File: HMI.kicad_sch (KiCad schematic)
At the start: 180 parts, among them J702 1050171001 Micro Type B, J703 Conn_01x04_Pin, J704 Conn_01x04_Pin, J705 Conn_01x14_Pin, J706 Header, J707 HX JN1.27-2x5 WZ H4.9, J708 HX JN1.27-2x5 WZ H4.9, SW701 EncSw, SW702 EncSw, SW703 EncSw, U701 STM32G431K8Tx, Y701 20 MHz

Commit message: Refactoring sch
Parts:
- removed P707: ~, symbol personal:Cosmetic_PWR_SRC
- removed P708: ~, symbol personal:Cosmetic_OUT
- removed P709, P712, P713: ~, symbol personal:Cosmetic_IN
- removed P711: ~, symbol personal:Cosmetic_IO
- removed P717, P718: ~, symbol personal:Cosmetic_GND2
- added J701: ZHOURI DC3, Connector_IDC:IDC-Header_2x05_P2.54mm_Horizontal, symbol Connector_Generic:Conn_02x05_Odd_Even
- added JP701: 0R, Resistor_THT:R_Axial_DIN0204_L3.6mm_D1.6mm_P5.08mm_Horizontal, symbol Device:R
- added P1: ~, symbol personal:Cosmetic_PWR
- added P10, P11, P2, P9: ~, symbol personal:Cosmetic_GND2
- added P3: ~, symbol personal:Cosmetic_PWR_SRC
- added P4: ~, symbol personal:Cosmetic_OUT
- added P5, P7, P8: ~, symbol personal:Cosmetic_IN
- added P6: ~, symbol personal:Cosmetic_IO
- added R701: 10k, Resistor_SMD:R_0603_1608Metric_Pad0.98x0.95mm_HandSolder, symbol Device:R
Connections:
- net Earth: now also JP701.2
- net GND: now also J701.5 (Pin_5), P10.1, P11.1, P2.1, P9.1
- net LV_NRST: now also J701.9 (Pin_9), P8.1, R701.2
- net LV_RX: now also J701.1 (Pin_1), P4.1
- net LV_SWDCLK: now also J701.10 (Pin_10), P7.1
- net LV_SWDIO: now also J701.8 (Pin_8), P6.1
- net LV_TX: now also J701.3 (Pin_3), P5.1
- net SL3: now also J701.6 (Pin_6), P1.1, P3.1, R701.1
- new net: J701.2 (Pin_2), JP701.1
- no-connect marks 9 -> 11
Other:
- note added: "INTERFACE TO MAIN BOARD"
- note added: "SWD header - Main board"
- note removed: "BLOCK INTERFACE"
- note removed: "SWD header - Main"
- moved on the sheet: C701, C702, C703, C704, C705, C706, C707, C708, C709, C711, C712, J706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

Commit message: sch refactoring complete
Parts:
- removed P10, P11, P2, P710, P719, P720, P721, P722, P723, P724, P725, P726, P727, P735, P737, P738, P740, P741, P742, P743, P778, P779, P780, P783, P785, P787, P788, P795, P796, P797, P798, P806, P9: ~, symbol personal:Cosmetic_GND2
- added H701, H702, H703, H704, H705, H706, H707, H708: MountingHole, MountingHole:MountingHole_3.2mm_M3, symbol Mechanical:MountingHole
- JP702, JP705, JP708, JP715: symbol Device:R -> Jumper:Jumper_2_Small_Bridged
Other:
- note added: "Board mounting"
- note removed: "HMI 700"
- title: Sheet Title A -> HMI
- moved on the sheet: C701, C702, C703, C704, C705, C706, C707, C708, C709, C710, C711, C712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

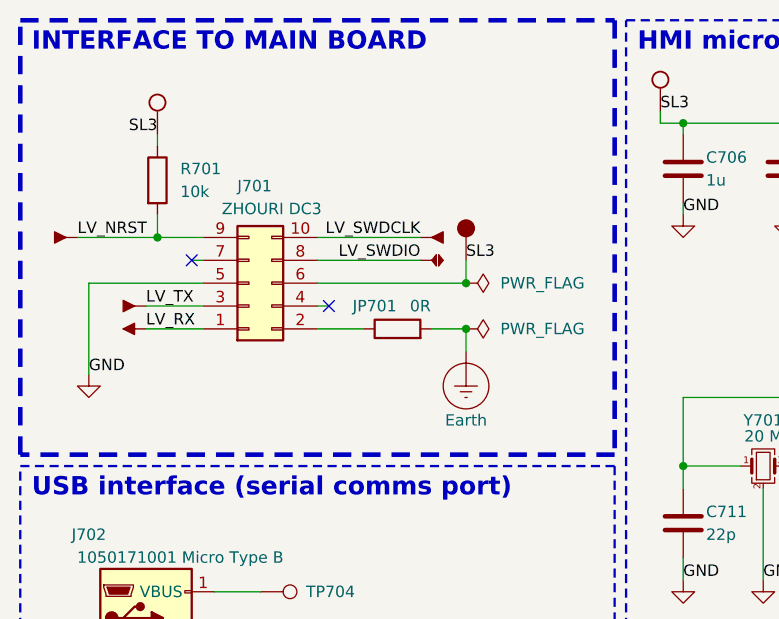
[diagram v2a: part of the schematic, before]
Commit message: Migrated PCB file to template, switched to preliminary
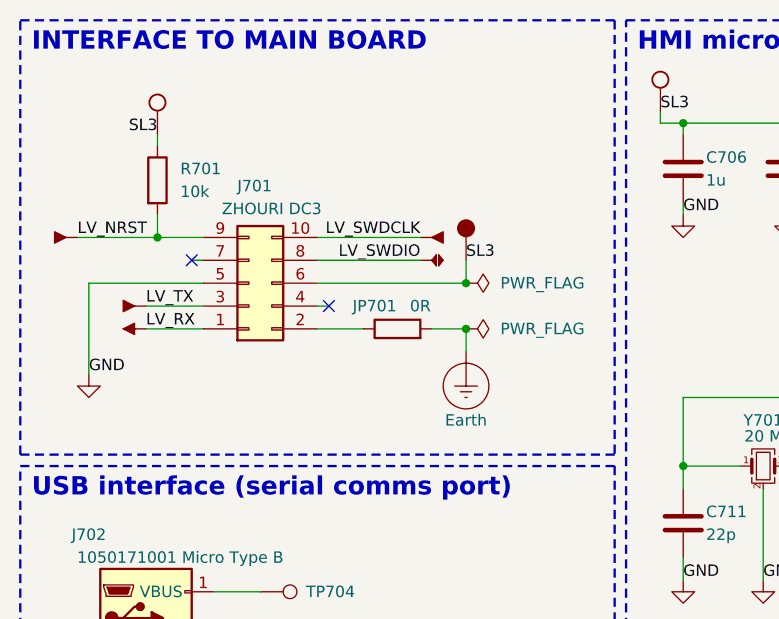
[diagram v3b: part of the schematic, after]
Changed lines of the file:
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@@
 		(end 80.01 62.23)
 		(stroke
-			(width 0.508)
+			(width 0.254)
 			(type dash)
 			(color 0 0 0 1)

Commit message: TFT 3D added
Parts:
- C710, OLED701: now not fitted
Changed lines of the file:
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@@
 		(in_bom yes)
 		(on_board yes)
-		(dnp no)
+		(dnp yes)
 		(property "Reference" "C710"
 			(at 198.12 41.9099 0)
@@
 		(in_bom yes)
 		(on_board yes)
-		(dnp no)
+		(dnp yes)
 		(property "Reference" "OLED701"
 			(at 219.71 17.78 0)

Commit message: Added code, pictures, readme, updated sch size and notes, changed to checked
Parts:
- D701: Manufacturer (none) -> Generic; Manufacturer Part Number (none) -> Generic 3 mm LED; now not fitted
- D702: Manufacturer (none) -> Osram; Manufacturer Part Number (none) -> LH T6MF-GGHH-1-E3L3
- JP701, JP703, JP708, JP710, JP713, JP714, JP715: Manufacturer (none) -> Generic; Manufacturer Part Number (none) -> Hand cut wire
- JP702, JP704, JP705, JP706, JP707, JP709, JP711, JP712, JP716: Manufacturer (none) -> Yageo; Manufacturer Part Number (none) -> RC0603JR-130RP

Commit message: Preparing release
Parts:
- J703: now not fitted
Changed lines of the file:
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@@
 		(in_bom yes)
 		(on_board yes)
-		(dnp no)
+		(dnp yes)
 		(property "Reference" "J703"
 			(at 217.17 43.18 0)
